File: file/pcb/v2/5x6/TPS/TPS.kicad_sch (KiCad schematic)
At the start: 106 parts, among them J1 I2C, J2 FFC-0.5mm, 12p, J3 FFC-0.5mm, 12p, J4 PH2.0-2pin, J5 FFC-0.5mm, 6p, J6 FFC-0.5mm, 6p, K1 SW_Push, K10 SW_Push, K11 SW_Push, K12 SW_Push, K13 SW_Push, K14 SW_Push, K15 SW_Push, K16 SW_Push, K17 SW_Push, K18 SW_Push, K19 SW_Push, K2 SW_Push, K20 SW_Push, K21 SW_Push, K22 SW_Push, K23 SW_Push, K24 SW_Push, K25 EC-11, K26 SW_Push, K27 SW_Push, K28 SW_Push, K29 SW_Push, K3 SW_Push, K30 SW_Push, K31 SW_Push, K4 SW_Push, K5 SW_Push, K6 SW_Push, K7 SW_Push, K8 SW_Push, K9 SW_Push, SW1 SW_Push, SW2 MSKT-12D14, SW3 MSKT-12D14, T1 AudioJack4, T2 AudioJack4, U1 MCU_ProMicro_13p

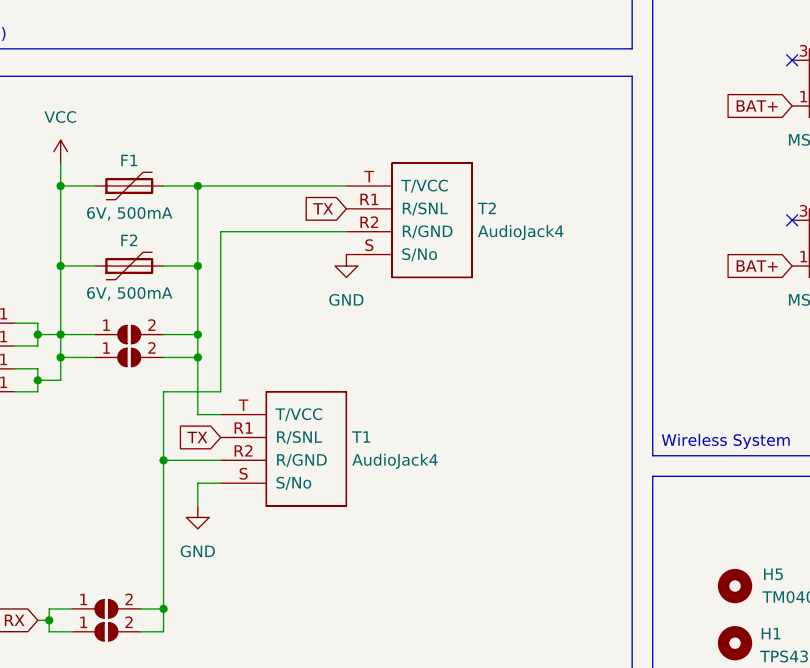
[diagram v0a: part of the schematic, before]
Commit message: fix TRRS TX/RX pins
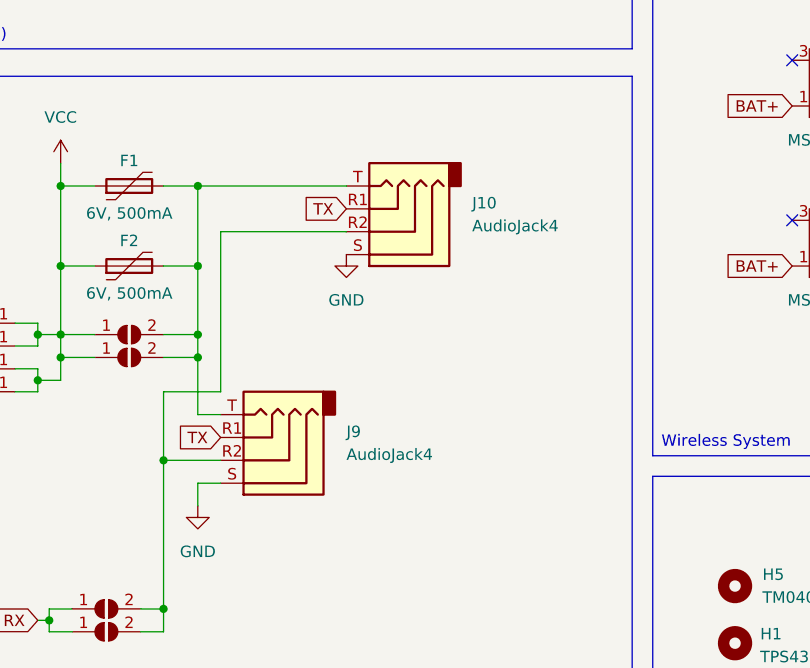
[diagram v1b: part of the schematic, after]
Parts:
- removed T1, T2: AudioJack4, DreaM117er-keebLibrary:TRRS-PJ-320A, dual side x2, symbol DreaM117er_Library:TRRS
- added J10, J9: AudioJack4, DreaM117er-keebLibrary:TRRS-PJ-320A, dual side x2, symbol Connector_Audio:AudioJack4
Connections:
- net GND: now also J10.S, J9.S
- net TX: now also J10.R1, J9.R1
- net at F1.2, F2.2, JP15.2 (B)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: now also J10.T, J9.T
- net at JP13.2 (B), JP14.2 (B): now also J10.R2, J9.R2
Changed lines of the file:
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@@
 	)
 	(symbol
+		(lib_id "Connector_Audio:AudioJack4")
+		(at 160.02 123.19 180)
+		(unit 1)
+		(exclude_from_sim no)
+		(in_bom yes)
+		(on_board yes)
+		(dnp no)
+		(fields_autoplaced yes)
+		(property "Reference" "J9"
+			(at 168.91 120.0149 0)
+			(effects
+				(font
+					(size 1.27 1.27)
+				)
+				(justify right)
+			)
+		)
+		(property "Value" "AudioJack4"
+			(at 168.91 122.5549 0)
+			(effects
+				(font
+					(size 1.27 1.27)
+				)
+				(justify right)
+			)
+		)
+		(property "Footprint" "DreaM117er-keebLibrary:TRRS-PJ-320A, dual side x2"
+			(at 160.02 123.19 0)
+			(effects
+				(font
+					(size 1.27 1.27)
+				)
+				(hide yes)
+			)
+		)
+		(property "Datasheet" "~"
+			(at 160.02 123.19 0)
+			(effects
+				(font
+					(size 1.27 1.27)
+				)
+				(hide yes)
+			)
+		)
+		(property "Description" "Audio Jack, 4 Poles (TRRS)"
+			(at 160.02 123.19 0)
+			(effects
+				(font
+					(size 1.27 1.27)
+				)
+				(hide yes)
+			)
+		)
+		(pin "R1"
+		)
+		(pin "T"
+		)
+		(pin "R2"
+		)
+		(pin "S"
+		)
+		(instances
+			(project ""
+				(path "/362e52b9-ba3a-40a2-a3a5-9227c3d95473"
+					(reference "J9")
+					(unit 1)
+				)
+			)
+		)
+	)
+	(symbol
 		(lib_id "Device:Polyfuse")
 		(at 144.78 101.6 90)
@@
 	)
 	(symbol
+		(lib_id "Connector_Audio:AudioJack4")
+		(at 173.99 97.79 180)
+		(unit 1)
+		(exclude_from_sim no)
+		(in_bom yes)
+		(on_board yes)
+		(dnp no)
+		(fields_autoplaced yes)
+		(property "Reference" "J10"
+			(at 182.88 94.6149 0)
+			(effects
+				(font
+					(size 1.27 1.27)
+				)
+				(justify right)
+			)
+		)
+		(property "Value" "AudioJack4"
+			(at 182.88 97.1549 0)
+			(effects
+				(font
+					(size 1.27 1.27)
+				)
+				(justify right)
+			)
+		)
+		(property "Footprint" "DreaM117er-keebLibrary:TRRS-PJ-320A, dual side x2"
+			(at 173.99 97.79 0)
+			(effects
+				(font
+					(size 1.27 1.27)
+				)
+				(hide yes)
+			)
+		)
+		(property "Datasheet" "~"
+			(at 173.99 97.79 0)
+			(effects
+				(font
+					(size 1.27 1.27)
+				)
+				(hide yes)
+			)
+		)
+		(property "Description" "Audio Jack, 4 Poles (TRRS)"
+			(at 173.99 97.79 0)
+			(effects
+				(font
+					(size 1.27 1.27)
+				)
+				(hide yes)
+			)
+		)
+		(pin "R1"
+		)
+		(pin "T"
+		)
+		(pin "R2"
+		)
+		(pin "S"
+		)
+		(instances
+			(project "TPS"
+				(path "/362e52b9-ba3a-40a2-a3a5-9227c3d95473"
+					(reference "J10")
+					(unit 1)
+				)
+			)
+		)
+	)
+	(symbol
 		(lib_id "Connector:Conn_01x07_Socket")
 		(at 87.63 181.61 0)
@@
 					(unit 1)
 				)
-			)
-		)
-	)
-	(symbol
-		(lib_name "TRRS_1")
-		(lib_id "DreaM117er_Library:TRRS")
-		(at 177.8 102.87 0)
-		(unit 1)
-		(exclude_from_sim no)
-		(in_bom yes)
-		(on_board yes)
-		(dnp no)
-		(fields_autoplaced yes)
-		(property "Reference" "T2"
-			(at 183.515 95.25 0)
-			(effects
-				(font
-					(size 1.27 1.27)
-				)
-				(justify left)
-			)
-		)
-		(property "Value" "AudioJack4"
-			(at 183.515 97.79 0)
-			(effects
-				(font
-					(size 1.27 1.27)
-				)
-				(justify left)
-			)
-		)
-		(property "Footprint" "DreaM117er-keebLibrary:TRRS-PJ-320A, dual side x2"
-			(at 177.8 106.68 0)
-			(effects
-				(font
-					(size 1.524 1.524)
-				)
-				(hide yes)
-			)
-		)
-		(property "Datasheet" "~"
-			(at 177.8 104.14 0)
-			(effects
-				(font
-					(size 1.524 1.524)
-				)
-				(hide yes)
-			)
-		)
-		(property "Description" ""
-			(at 177.8 102.87 0)
-			(effects
-				(font
-					(size 1.27 1.27)
-				)
-			)
-		)
-		(pin "T"
-		)
-		(pin "R2"
-		)
-		(pin "S"
-		)
-		(pin "R1"
-		)
-		(instances
-			(project "TPS"
-				(path "/362e52b9-ba3a-40a2-a3a5-9227c3d95473"
-					(reference "T2")
-					(unit 1)
-				)
-			)
-		)
-	)
-	(symbol
-		(lib_name "TRRS_1")
-		(lib_id "DreaM117er_Library:TRRS")
-		(at 163.83 128.27 0)
-		(unit 1)
-		(exclude_from_sim no)
-		(in_bom yes)
-		(on_board yes)
-		(dnp no)
-		(fields_autoplaced yes)
-		(property "Reference" "T1"
-			(at 169.545 120.65 0)
-			(effects
-				(font
-					(size 1.27 1.27)
-				)
-				(justify left)
-			)
-		)
-		(property "Value" "AudioJack4"
-			(at 169.545 123.19 0)
-			(effects
-				(font
-					(size 1.27 1.27)
-				)
-				(justify left)
-			)
-		)
-		(property "Footprint" "DreaM117er-keebLibrary:TRRS-PJ-320A, dual side x2"
-			(at 163.83 132.08 0)
-			(effects
-				(font
-					(size 1.524 1.524)
-				)
-				(hide yes)
-			)
-		)
-		(property "Datasheet" "~"
-			(at 163.83 129.54 0)
-			(effects
-				(font
-					(size 1.524 1.524)
-				)
-				(hide yes)
-			)
-		)
-		(property "Description" ""
-			(at 163.83 128.27 0)
-			(effects
-				(font
-					(size 1.27 1.27)
-				)
-			)
-		)
-		(pin "T"
-		)
-		(pin "R2"
-		)
-		(pin "S"
-		)
-		(pin "R1"
-		)
-		(instances
-			(project "TPS"
-				(path "/362e52b9-ba3a-40a2-a3a5-9227c3d95473"
-					(reference "T1")
-					(unit 1)
-				)

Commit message: fix main PCB file UI
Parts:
- J10: footprint DreaM117er-keebLibrary:TRRS-PJ-320A, dual side x2 -> DreaM117er-keebLibrary:TRRS-PJ-320A, dual side x2_3rd
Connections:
- net N/A1: now reaches SW2.3 (C)
- net N/A2: now reaches SW3.3 (C)
- no-connect marks 22 -> 20
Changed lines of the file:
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@@
 	)
 	(no_connect
-		(at 218.44 78.74)
-	)
-	(no_connect
 		(at 41.91 184.15)
 	)
@@
 	)
 	(no_connect
-		(at 218.44 96.52)
-	)
-	(no_connect
 		(at 82.55 158.75)
 	)
@@
 		)
 	)
+	(global_label "N{slash}A1"
+		(shape input)
+		(at 218.44 78.74 180)
+		(fields_autoplaced yes)
+		(effects
+			(font
+				(size 1.27 1.27)
+			)
+			(justify right)
+		)
+		(property "Intersheetrefs" "${INTERSHEET_REFS}"
+			(at 210.4957 78.74 0)
+			(effects
+				(font
+					(size 1.27 1.27)
+				)
+				(justify right)
+				(hide yes)
+			)
+		)
+	)
+	(global_label "N{slash}A2"
+		(shape input)
+		(at 218.44 96.52 180)
+		(fields_autoplaced yes)
+		(effects
+			(font
+				(size 1.27 1.27)
+			)
+			(justify right)
+		)
+		(property "Intersheetrefs" "${INTERSHEET_REFS}"
+			(at 210.4957 96.52 0)
+			(effects
+				(font
+					(size 1.27 1.27)
+				)
+				(justify right)
+				(hide yes)
+			)
+		)
+	)
 	(global_label "col5"
 		(shape input)
@@
 			)
 		)
-		(property "Footprint" "DreaM117er-keebLibrary:TRRS-PJ-320A, dual side x2"
+		(property "Footprint" "DreaM117er-keebLibrary:TRRS-PJ-320A, dual side x2_3rd"
 			(at 173.99 97.79 0)
 			(effects
